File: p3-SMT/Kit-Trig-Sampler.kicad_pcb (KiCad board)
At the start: 2 copper layers, 78 x 109.2 mm, 81 parts, among them J1 START_CV, J10 AUDIO_INR, J11 AUDIO_OUTL, J13 BANK_CV, J14 Eurorack_Power_10pin_Unshroud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, J2 LENGTH_CV, J3 SAMP_CV, J4 PITCH CV, J5 REV_TRIG, J6 PLAY_TRIG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

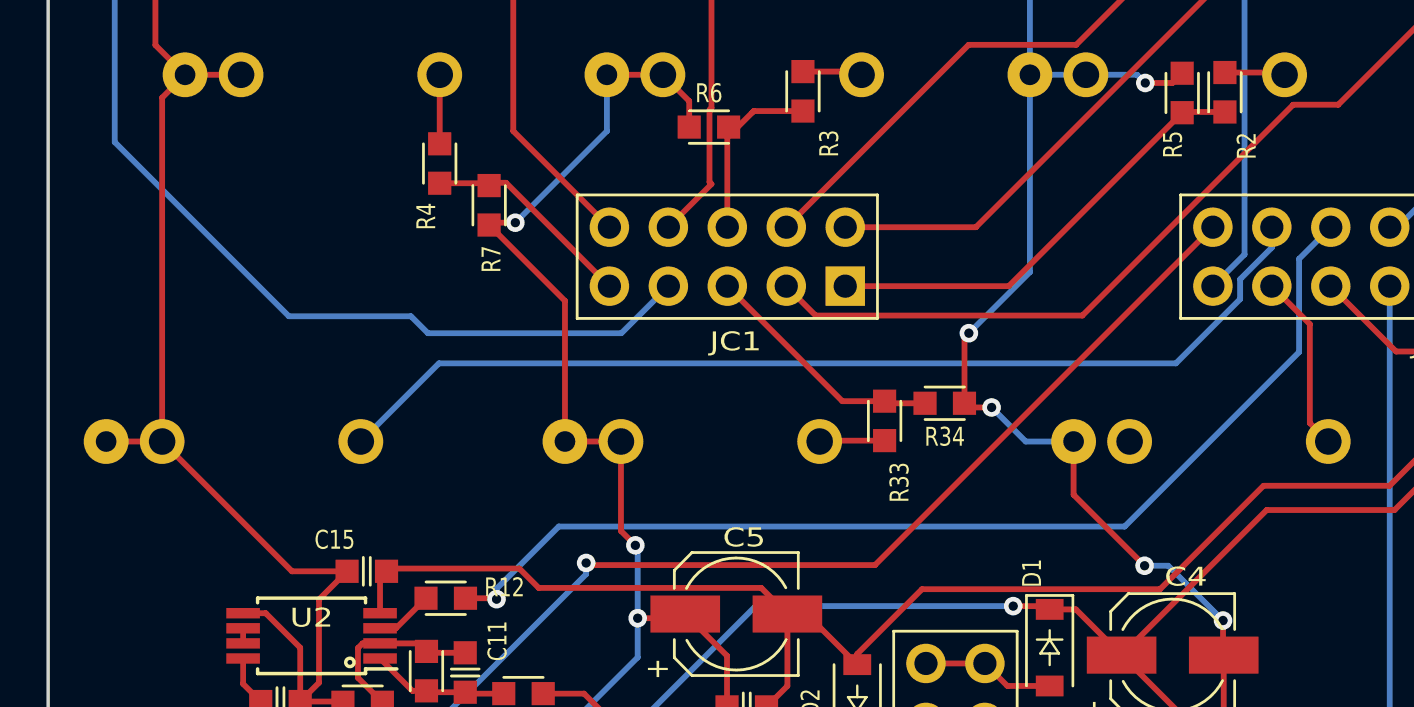
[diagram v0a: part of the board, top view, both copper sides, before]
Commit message: p3 SMT: added 47K resistors to Trig Ins
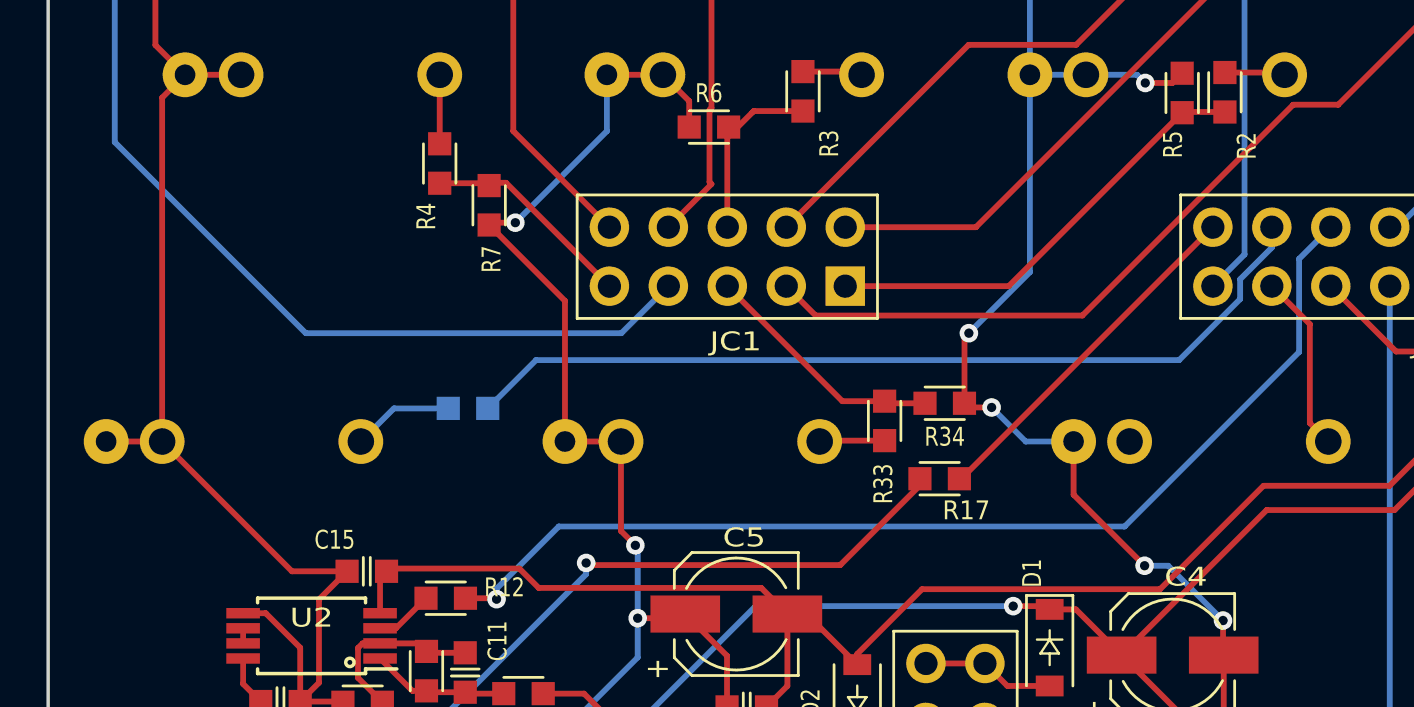
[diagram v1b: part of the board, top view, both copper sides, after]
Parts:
- added R17: 47k_0603, 4ms_Resistor:R_0603, F.Cu at (50.4, 99.9)
- added R20: 47k_0603, 4ms_Resistor:R_0603, B.Cu at (30.1, 96.8)
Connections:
- J5 pad 1: /D2 -> Net-(J5-SIG)
- J6 pad 1: /D13 -> Net-(J6-SIG)
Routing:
- net /D2: track 47.3 -> 15.3 mm, vias 1 -> 0
- net Net-(J5-SIG): track 0.00 -> 30.1 mm, vias 0 -> 1
- net /D13: track 44.1 -> 38.0 mm
- net Net-(J6-SIG): track 0.00 -> 4.36 mm

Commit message: p3 smt: generated prod files
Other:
- board text added: "SAMPLER-SMT-p3"
- board text removed: "SAMPLER-SMT-p2"
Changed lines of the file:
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@@
     (effects (font (size 1 1) (thickness 0.15)) (justify right top mirror))
   )
-  (gr_text "SAMPLER-SMT-p2" (at 49.82 51.14) (layer "F.SilkS")
+  (gr_text "SAMPLER-SMT-p3" (at 49.82 51.14) (layer "F.SilkS")
     (effects (font (size 1.27 1.27) (thickness 0.254) bold italic))
   )
